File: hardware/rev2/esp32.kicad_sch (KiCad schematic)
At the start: 31 parts, among them SW1 SW_Push, U3 ESP32-S3, Y2 Crystal_GND24

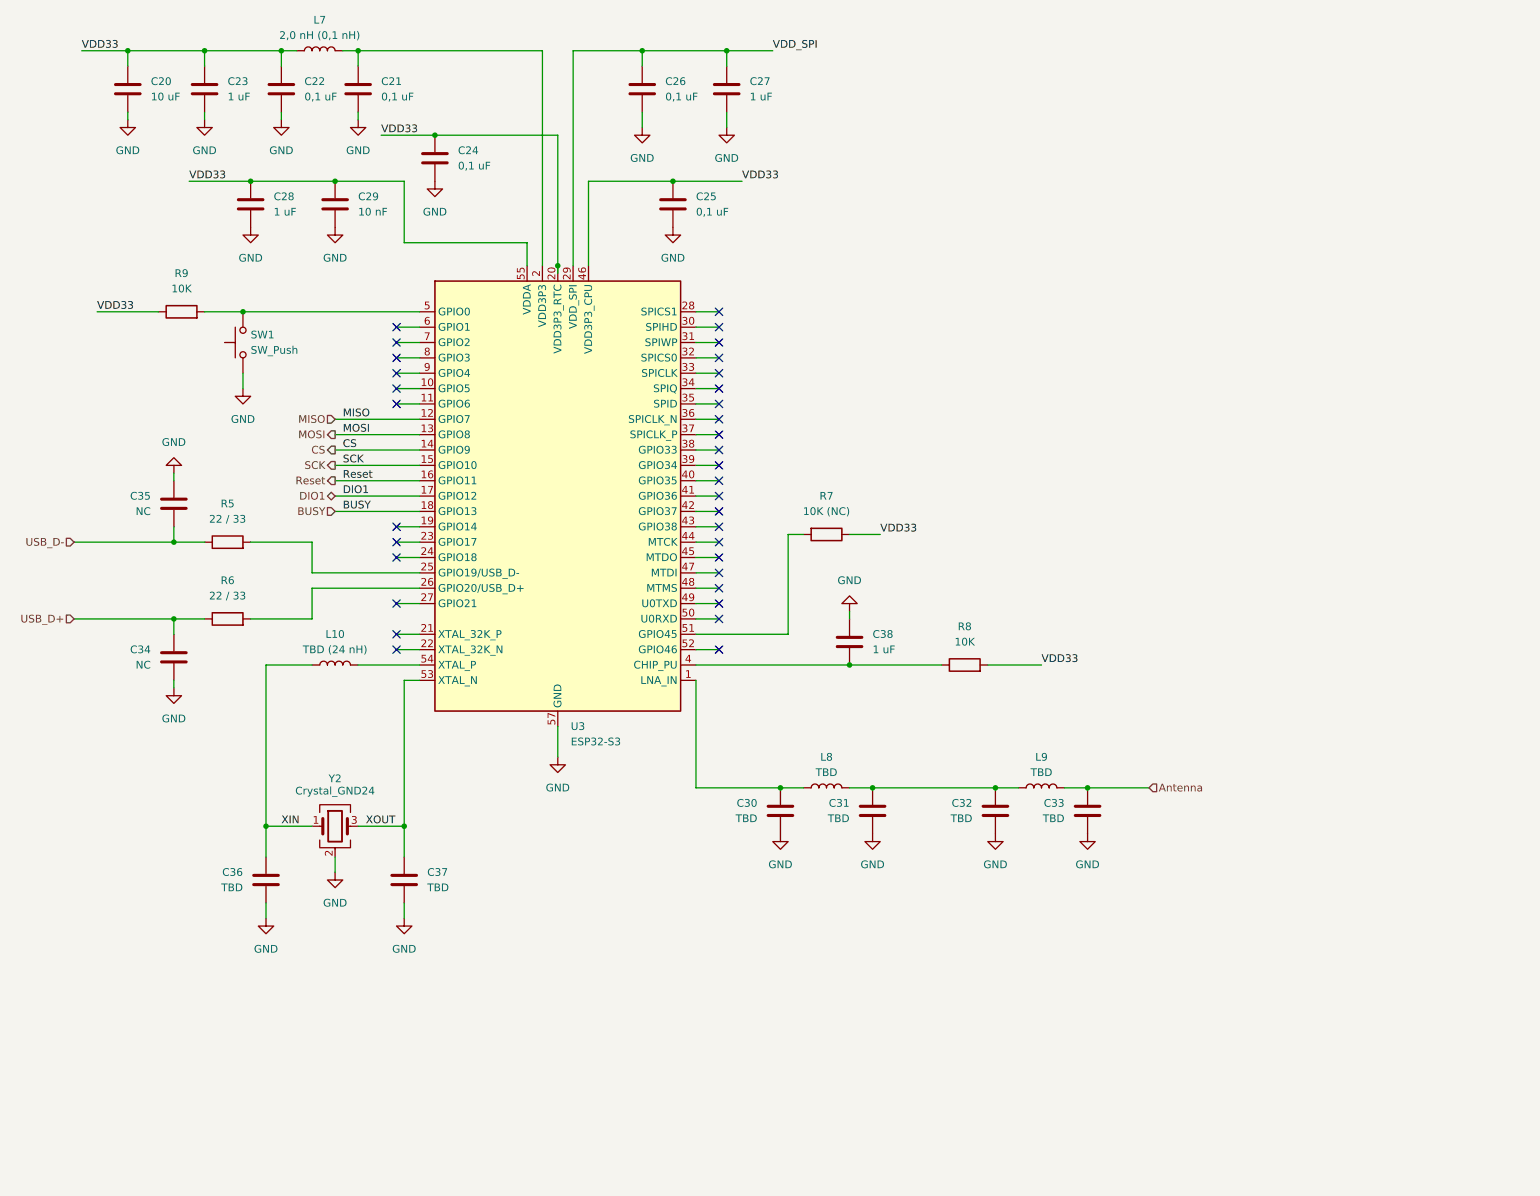
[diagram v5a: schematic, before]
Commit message: cleaned up esp32 and added antenna stuff on main sheet
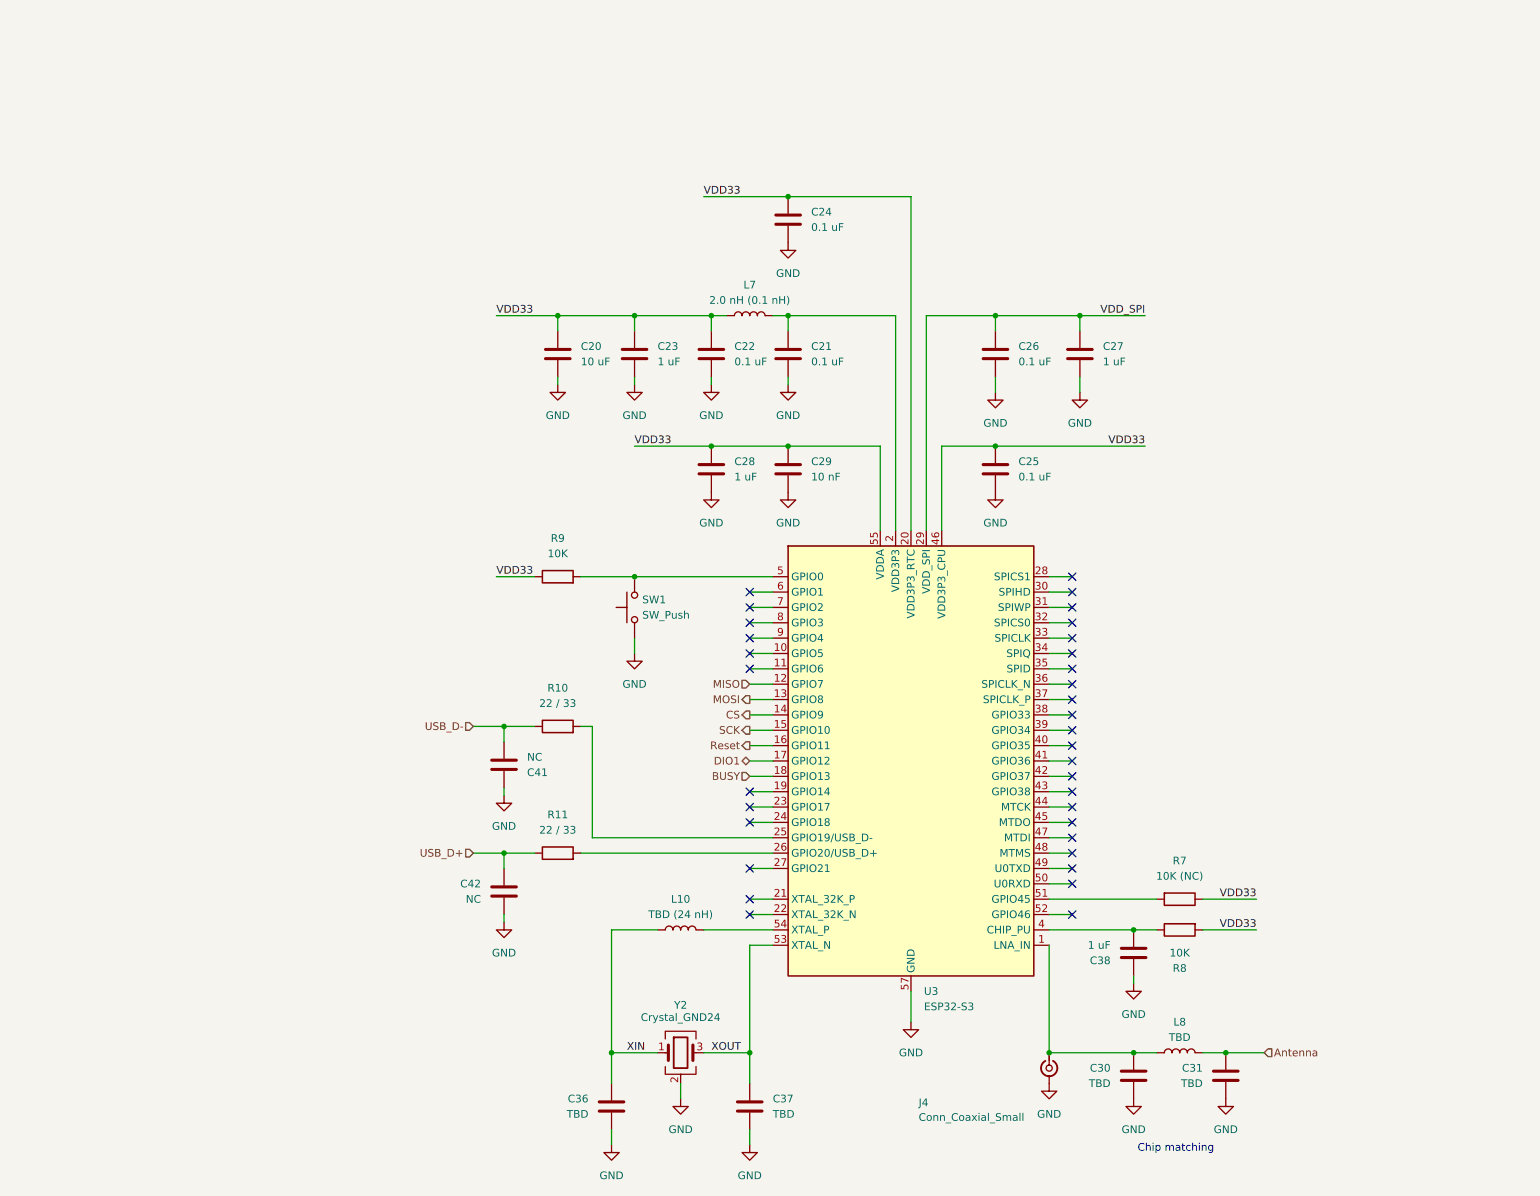
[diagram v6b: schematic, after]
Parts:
- removed C32, C33: TBD, symbol Device:C
- removed C34, C35: NC, symbol Device:C
- removed L9: TBD, symbol Device:L
- removed R5, R6: 22 / 33, symbol Device:R
- added C41, C42: NC, symbol Device:C
- added J4: Conn_Coaxial_Small, symbol Connector:Conn_Coaxial_Small
- added R10, R11: 22 / 33, symbol Device:R
- C21, C22, C24, C25, C26: value 0,1 uF -> 0.1 uF
- L7: value 2,0 nH (0,1 nH) -> 2.0 nH (0.1 nH)
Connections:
- net Antenna: now also C31.1, L8.1
- net GND: now also C41.2, C42.2, J4.2 (Ext)
- net USB_D+: now also C42.1, R11.1
- net USB_D-: now also C41.1, R10.1
- net at U3.26 (GPIO20/USB_D+): now also R11.2
- net at C30.1, L8.2, U3.1 (LNA_IN): now also J4.1 (In)
- net at U3.25 (GPIO19/USB_D-): now also R10.2
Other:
- note added: "Chip matching"
- moved on the sheet: C20, C21, C22, C23, C24, C25, C26, C27, C28, C29, C30, C31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

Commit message: added power, net classes and some antenna stuff
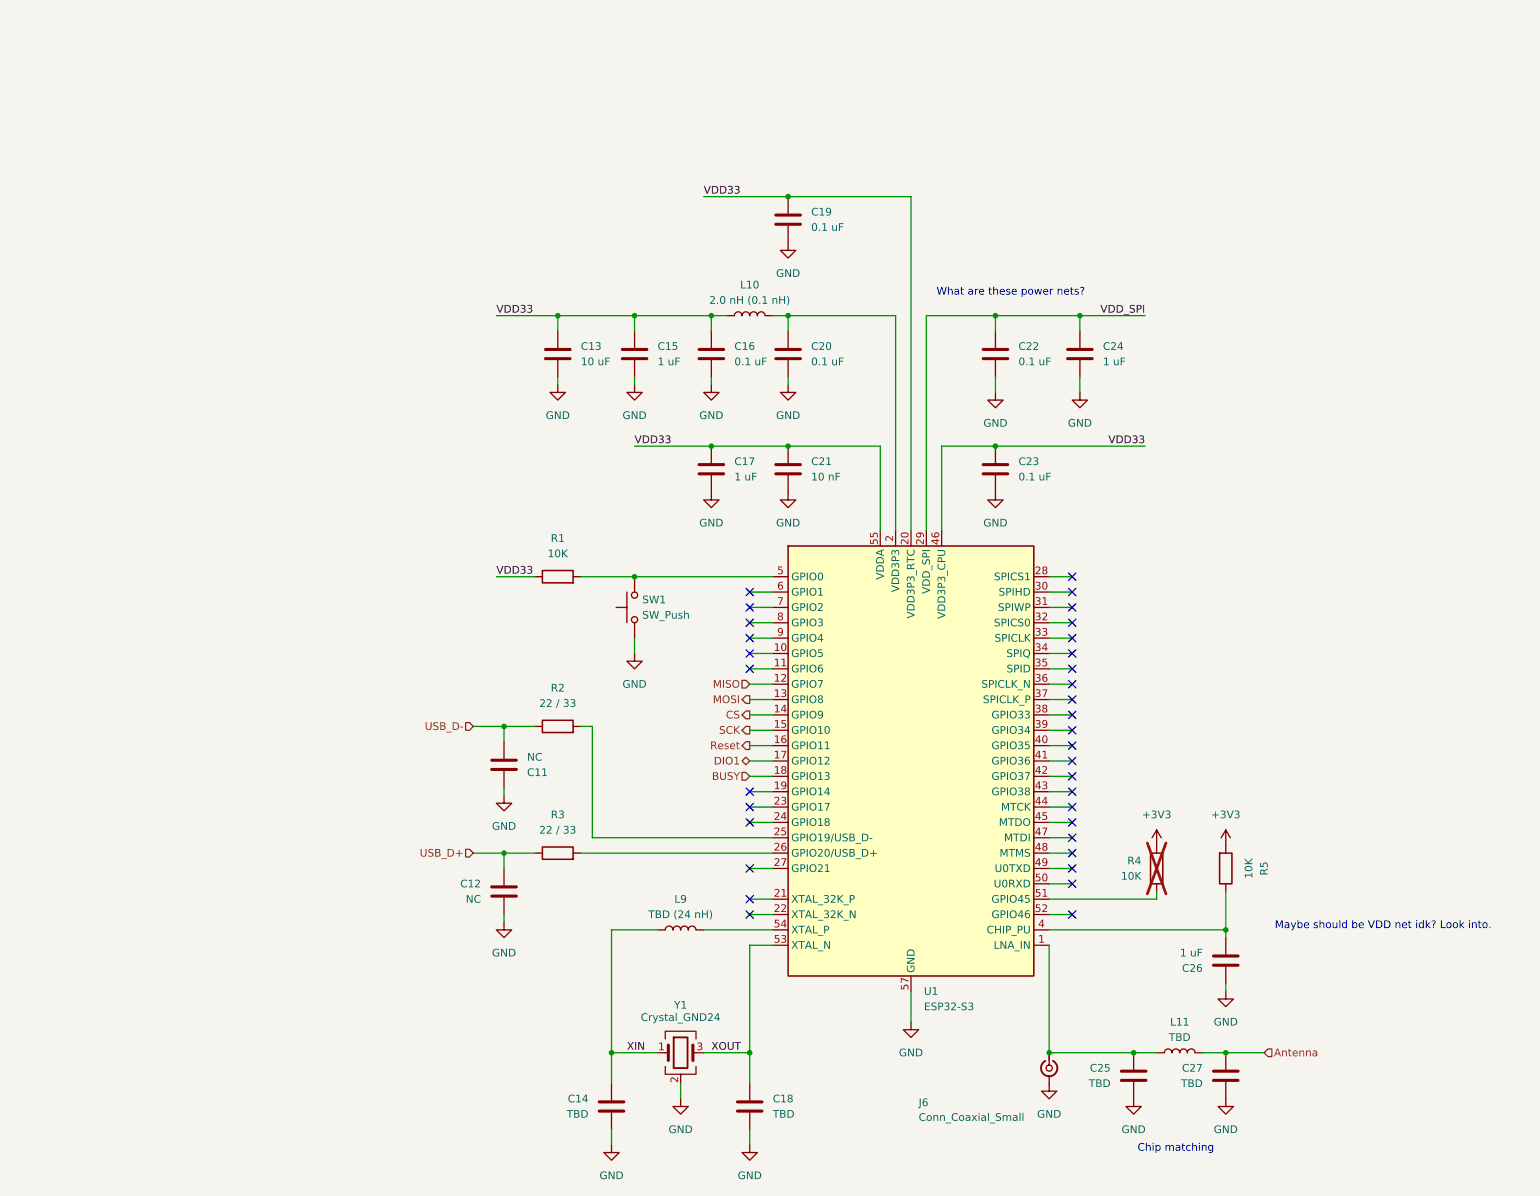
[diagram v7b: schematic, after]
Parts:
- R4: renamed from R7; value 10K (NC) -> 10K; now not fitted; now left out of the parts list
- renumbered C41 to C11, C42 to C12, C20 to C13, C36 to C14, C23 to C15, C22 to C16, C28 to C17, C37 to C18, C24 to C19, C21 to C20, C29 to C21, C26 to C22, C25 to C23, C27 to C24, C30 to C25, C38 to C26, C31 to C27, J4 to J6, L7 to L10, L8 to L11, L10 to L9, R9 to R1, R10 to R2, R11 to R3, R8 to R5, U3 to U1, Y2 to Y1
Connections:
- net VDD33: no longer R4.1, R5.2
- new net +3V3: R4.1, R5.2
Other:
- note added: "Maybe should be VDD net idk? Look into."
- note added: "What are these power nets?"
- moved on the sheet: C26, R5

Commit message: fixed some ERC errors and warnings, added USB, assigned a bunch of footprints
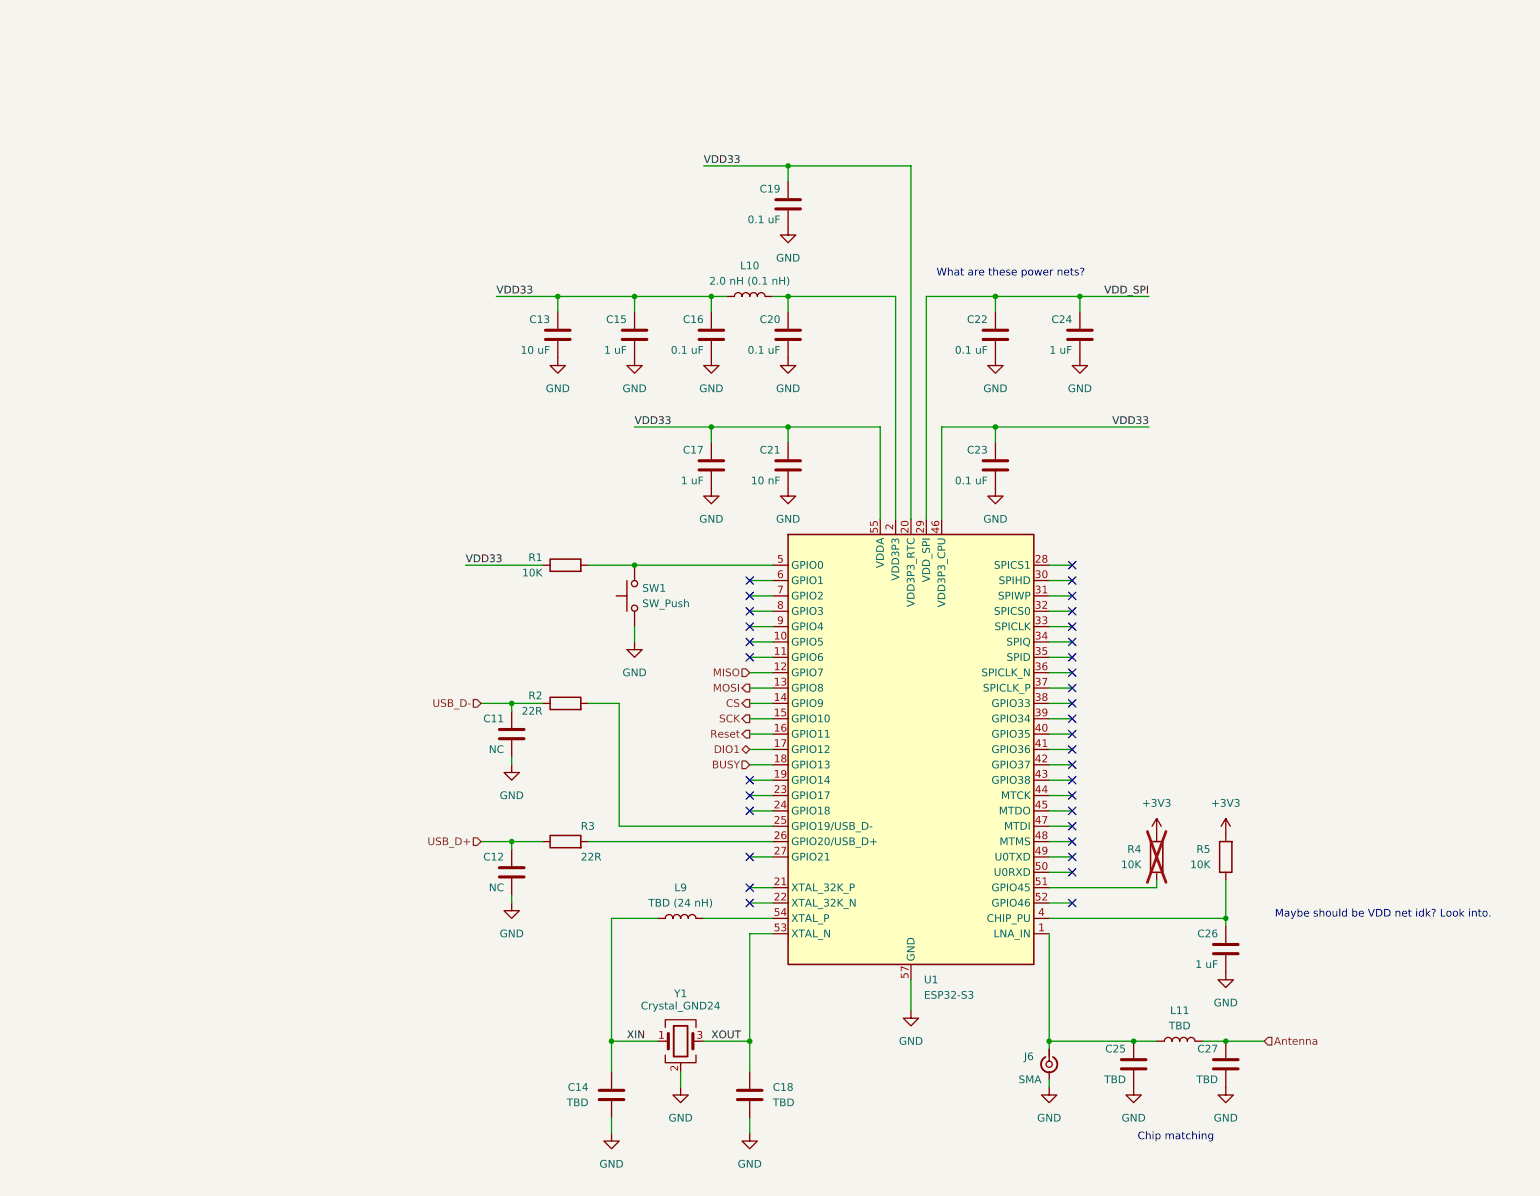
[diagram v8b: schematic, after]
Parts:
- C11, C12: footprint (none) -> Capacitor_SMD:C_0201_0603Metric_Pad0.64x0.40mm_HandSolder
- C13, C14, C15, C16, C17, C18, C19, C20, C21, C22, C23, C24, C26: footprint (none) -> Capacitor_SMD:C_0603_1608Metric_Pad1.08x0.95mm_HandSolder
- C25, C27: footprint (none) -> Capacitor_SMD:C_0402_1005Metric_Pad0.74x0.62mm_HandSolder
- J6: value Conn_Coaxial_Small -> SMA
- L10, L9, R1, R4, R5: footprint (none) -> Inductor_SMD:L_0603_1608Metric_Pad1.05x0.95mm_HandSolder
- L11: footprint (none) -> Inductor_SMD:L_0402_1005Metric_Pad0.77x0.64mm_HandSolder
- R2, R3: value 22 / 33 -> 22R; footprint (none) -> Inductor_SMD:L_0603_1608Metric_Pad1.05x0.95mm_HandSolder
- SW1: footprint (none) -> Button_Switch_SMD:SW_Push_1P1T_NO_CK_KSC7xxJ
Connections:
- net GND: now also C11.1; no longer C11.2
- net USB_D-: now also C11.2; no longer C11.1
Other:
- moved on the sheet: C11, C12, C13, C14, C15, C16, C17, C18, C19, C20, C21, C22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
